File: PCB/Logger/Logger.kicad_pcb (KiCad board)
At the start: 2 copper layers, 70 x 70 mm, 78 parts, among them J1 JST-PH-SM4-TB, J2 USB-C-Socket-V, J3 Conn_01x05, J4 Shelly, J5 USB-PROG, J6 TF_PUSH, Q1 CJ2301, Q2 C179347, Q3 CJ2301, U1 ESP32-S3-MINI-1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

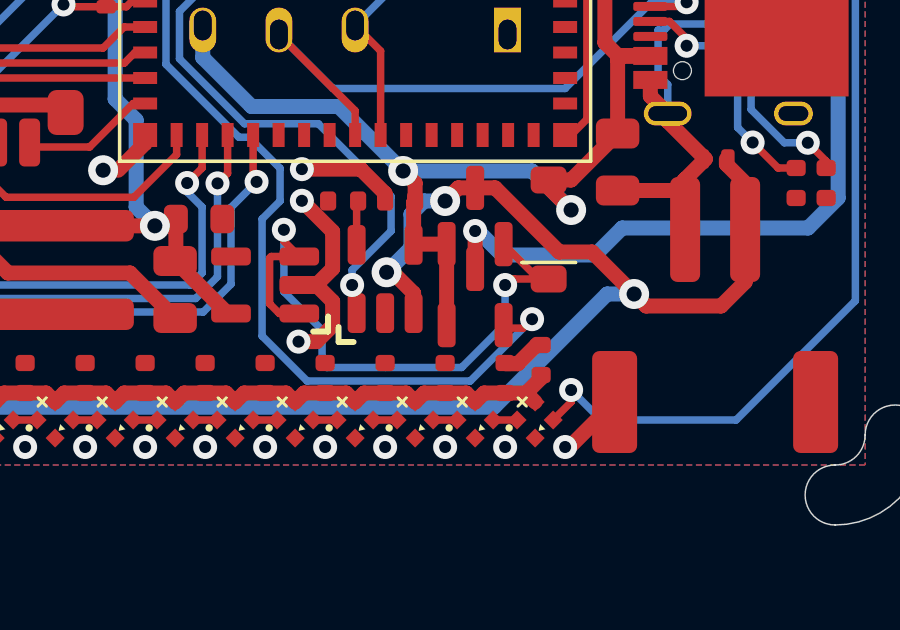
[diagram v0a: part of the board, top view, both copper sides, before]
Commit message: FFS USB not working
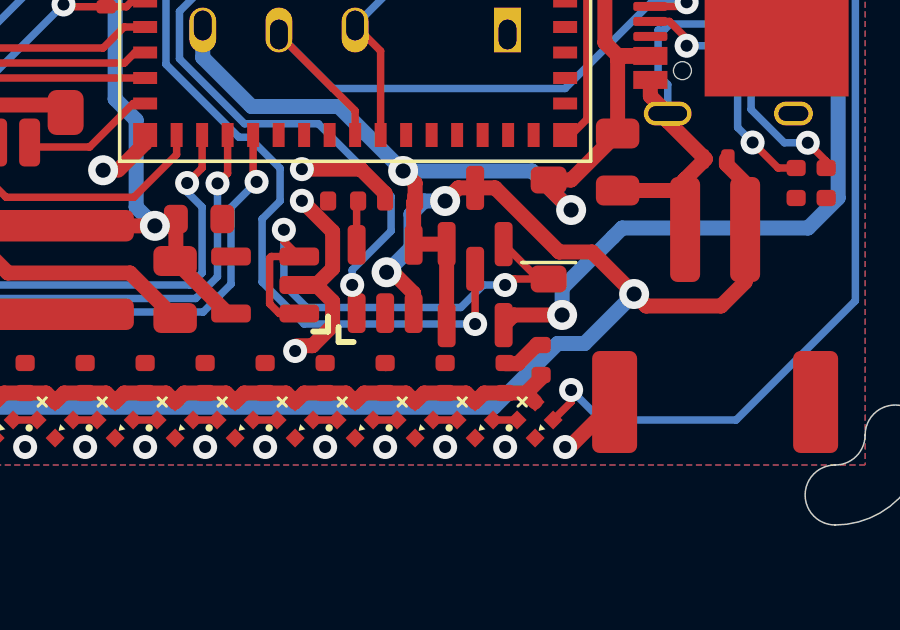
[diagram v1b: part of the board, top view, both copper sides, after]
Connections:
- Q3 pad 2: USB -> +3.3V
- Q3 pad 3: +3.3V -> USB
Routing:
- net USB: track 27.5 -> 23.7 mm
- net Net-(D2-K): track 20.9 -> 17.8 mm
- net +3.3V: track 88.2 -> 87.1 mm

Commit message: Tidy PCB
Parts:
- moved D4 0.22 mm to (95.2, 91.1), turned to 45 degrees
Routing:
- net RGB: track 8.07 -> 6.97 mm
- net GND: track 92.8 -> 92.1 mm
- net SPWR: track 90.9 -> 91.4 mm

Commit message: New headers
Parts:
- removed J5: USB-PROG, RevK:USB-PROG
- added J7: TC2030-USB-NL-DS, RevK:Tag-Connect_TC2030-IDC-NL_2x03_P1.27mm_Vertical, B.Cu at (89.2, 109.2)
- J4: value Shelly -> Reset; footprint RevK:Shelly -> RevK:AA-Pad
- moved J4 3.50 mm to (104.0, 98.0)
- moved R6 2.08 mm to (88.3, 110.2), turned to -90 degrees
- moved J2 1.39 mm to (114.9, 100.0)
- moved Q2 0.65 mm to (90.2, 109.7)
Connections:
- D24 pad 1: Net-(J4-0) -> Net-(U1-GPIO0)
- J4 pad 2: Net-(J4-0) -> Net-(J4-Pin_2)
- U1 pad 20: unconnected-(U1-GPIO16-Pad20) -> GND
- U1 pad 21: unconnected-(U1-GPIO17-Pad21) -> GND
- U1 pad 22: unconnected-(U1-GPIO18-Pad22) -> GND
- U1 pad 25: unconnected-(U1-GPIO21-Pad25) -> Net-(J4-Pin_2)
- U1 pad 39: Net-(J4-Tx) -> unconnected-(U1-GPIO43-Pad39)
- U1 pad 4: Net-(J4-0) -> Net-(U1-GPIO0)
- U1 pad 40: Net-(J4-Rx) -> unconnected-(U1-GPIO44-Pad40)
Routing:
- net GND: track 92.1 -> 143.0 mm, vias 37 -> 40
- net D+: track 19.7 -> 51.6 mm, vias 1 -> 3
- net VBUS: track 37.1 -> 65.2 mm
- net Net-(U1-GPIO0): track 0.00 -> 21.8 mm, vias 0 -> 2
- net D-: track 22.9 -> 40.6 mm, vias 1 -> 3
- net Net-(J4-0): track 17.5 -> 0.00 mm, vias 1 -> 0
- net +3.3V: track 87.1 -> 74.3 mm, vias 3 -> 5
- net Net-(J4-Pin_2): track 0.00 -> 9.70 mm, vias 0 -> 1
- net PWR: track 18.5 -> 27.9 mm
- net Net-(J4-Rx): track 7.14 -> 0.00 mm
- net ACCSCL: track 25.0 -> 30.5 mm
- net ACCSDA: track 22.4 -> 27.0 mm
- net Net-(J4-Tx): track 3.98 -> 0.00 mm
- net CHARGING: track 20.2 -> 16.9 mm
- net Net-(Q2-S): track 5.26 -> 6.41 mm
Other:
- board text added: "A"

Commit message: Resistors
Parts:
- added R15: 10K, RevK:R_0402, F.Cu at (93.1, 107.1)
- added R16: 10K, RevK:R_0402, F.Cu at (90.8, 107.0)
- added R17: 10K, RevK:R_0402, F.Cu at (88.0, 107.5)
- added R18: 10K, RevK:R_0402, F.Cu at (86.5, 107.0)
- added R19: 10K, RevK:R_0402, F.Cu at (85.5, 107.0)
- added R20: 10K, RevK:R_0402, F.Cu at (84.3, 107.0)
- moved D6 8.46 mm to (80.0, 111.7), turned to 0 degrees
- moved C18 2.57 mm to (85.3, 110.8)
- moved J6 2.45 mm to (86.6, 97.5)
- moved C21 1.76 mm to (83.2, 111.3), turned to 90 degrees
- moved R10 0.53 mm to (94.3, 110.0)
- moved Q2 0.40 mm to (90.2, 110.1)
- moved R6 0.22 mm to (88.2, 110.4)
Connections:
- J6 pad 1: unconnected-(J6-DAT2-Pad1) -> Net-(J6-DAT2)
- J6 pad 4: SPWR -> +3.3V
- J6 pad 8: unconnected-(J6-DAT1-Pad8) -> Net-(J6-DAT1)
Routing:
- net +3.3V: track 74.3 -> 93.2 mm
- net RGB: track 6.62 -> 17.4 mm
- net SPWR: track 91.8 -> 87.9 mm
- net SDMISO: track 8.94 -> 11.6 mm, vias 0 -> 2
- net SDSCK: track 9.74 -> 12.2 mm
- net Net-(J6-DAT1): track 0.00 -> 1.97 mm
- net SDSS: track 13.6 -> 14.9 mm
- net SDMOSI: track 12.2 -> 13.5 mm
- net Net-(J6-DAT2): track 0.00 -> 1.30 mm
- net GND: track 143.0 -> 141.9 mm, vias 40 -> 34
- net VBUS: track 65.2 -> 64.1 mm
